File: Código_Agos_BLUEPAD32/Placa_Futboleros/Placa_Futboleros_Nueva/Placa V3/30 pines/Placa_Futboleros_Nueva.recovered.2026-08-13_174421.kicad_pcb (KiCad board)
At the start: 2 copper layers, 52 x 100 mm, 19 parts, among them J1 BAT, J2 Motor_Izq_Adelante, J3 Motor_Izq_Atras, J4 Motor_Der_Adelante, J5 Motor_Der_Atras, U1 LM7805_TO220, U3 DRV8833, U4 DRV8833, U5 ESP32-DEVKIT-V1

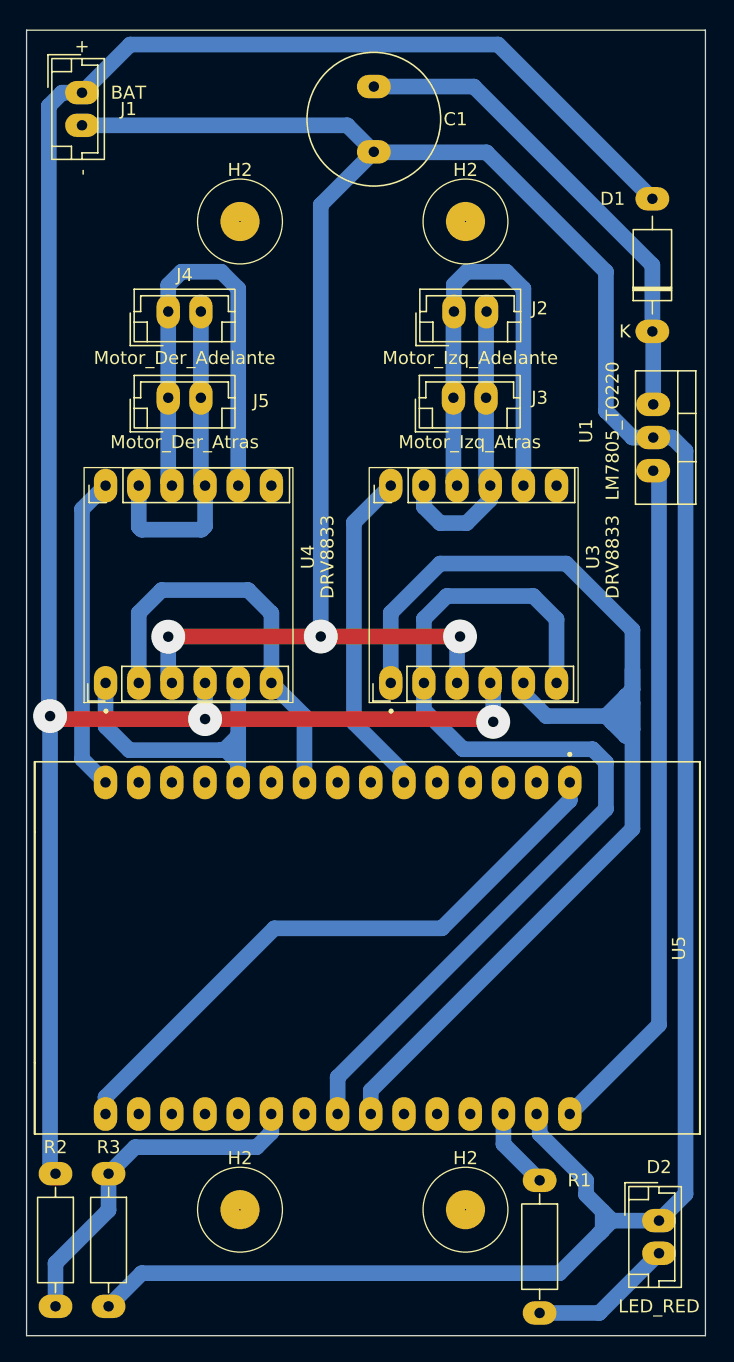
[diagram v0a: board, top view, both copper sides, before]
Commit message: Correección Kicad y ADC codigo
Se agrega adc al codigo y cambio en kicad ya que el NPTH mecanico arruino las redes
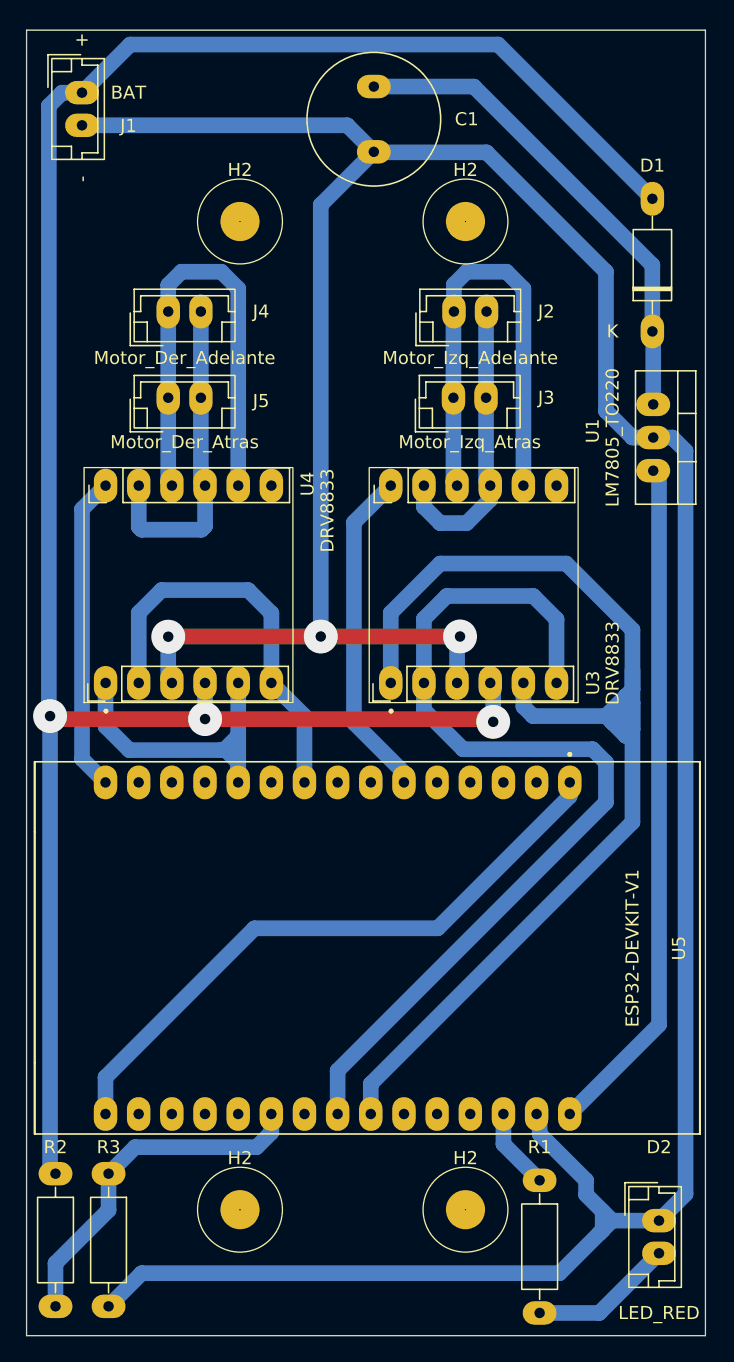
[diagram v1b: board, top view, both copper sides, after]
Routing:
- net (no net): track 0.00 -> 1002.3 mm, vias 0 -> 6
- net GND: track 248.3 -> 0.00 mm, vias 3 -> 0
- net VCC: track 175.0 -> 0.00 mm, vias 3 -> 0
- net IN_M1A: track 93.8 -> 0.00 mm
- net IN_M1B: track 74.5 -> 0.00 mm
- net +5V: track 52.3 -> 0.00 mm
- net +3.3V: track 47.6 -> 0.00 mm
- net Net-(D1-K): track 37.7 -> 0.00 mm
- net Net-(J2-Pin_1): track 36.9 -> 0.00 mm
- net Net-(J4-Pin_1): track 36.9 -> 0.00 mm
- net IN_M2B: track 31.0 -> 0.00 mm
- net /ADC: track 27.0 -> 0.00 mm
- net SLEEP_M1: track 25.5 -> 0.00 mm
- net IN_M2A: track 25.3 -> 0.00 mm
- net Net-(J4-Pin_2): track 25.0 -> 0.00 mm
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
